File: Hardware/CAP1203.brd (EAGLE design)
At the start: 38.1 x 25.4 mm, 41 parts, among them J1 Qwiic Right Angle, J2 Qwiic Right Angle, J3 Cap Touch Breakout Pins, J4 I2C Breakout Pins, U1 Cap Touch Slider, U2 CAP1203

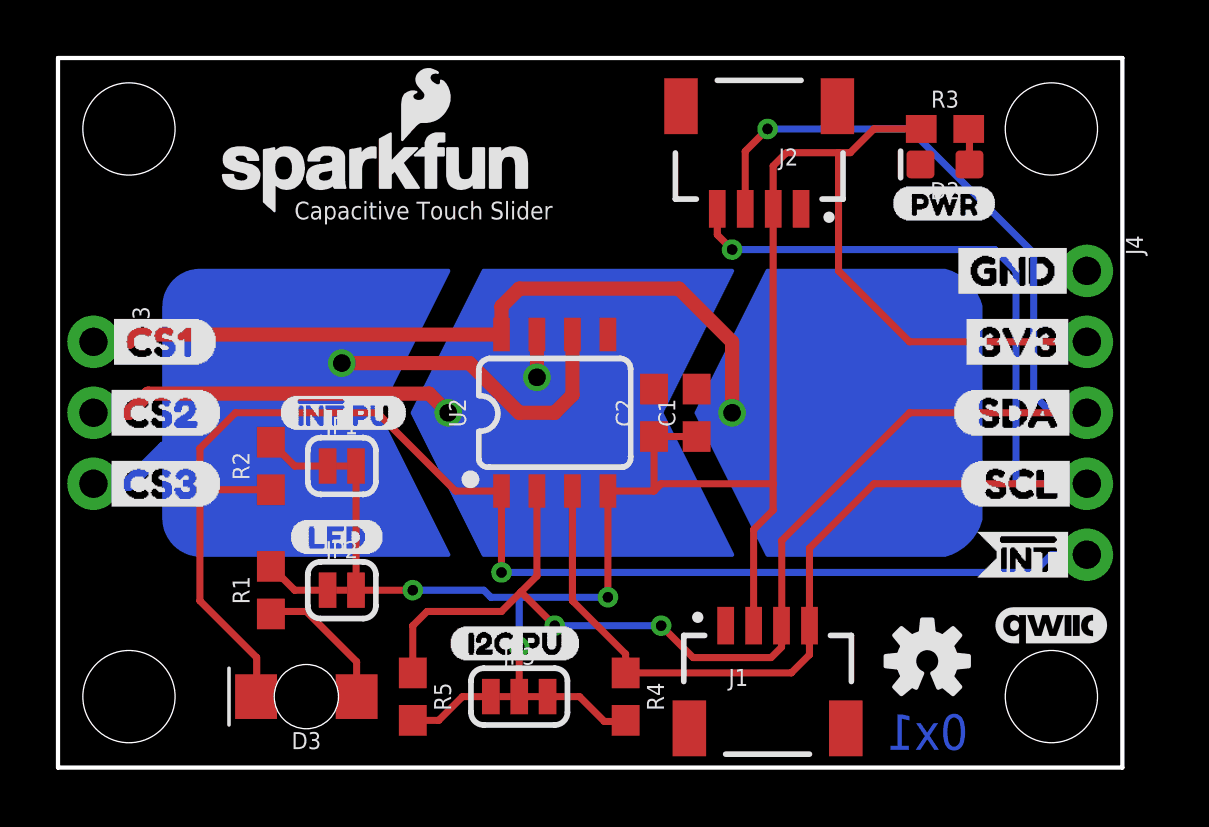
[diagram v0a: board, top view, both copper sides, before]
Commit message: Design review revisions
* Updated brd and sch to match SparkFun design standards
* Updated symbol to depict slider
* Updated silkscreen text
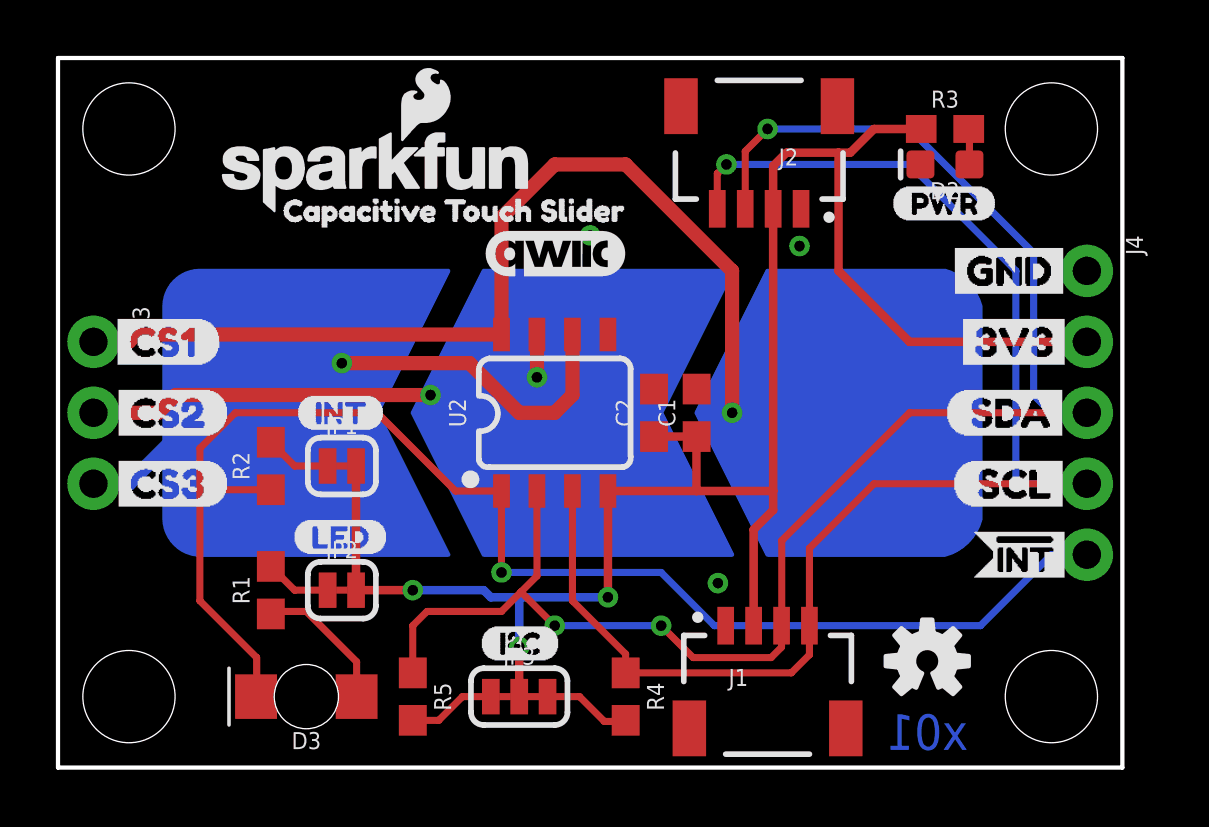
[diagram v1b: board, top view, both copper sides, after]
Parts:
- added U$17: QWIIC_LOGO_5MM, SparkFun-Aesthetics:QWIIC_5MM
- added U$3, U$5: (no value), buzzard_labels_title:CAPACITIVE_TOUCH_SLIDER0
- S1: value Cap Touch Slider -> (none)
- U$13: device buzzard_labels:PWR0 -> Labels:I_SUPER2_C-()-03
- U$14: device buzzard_labels:I2C_PU1 -> buzzard_labels (4):INT0
- U$15: device buzzard_labels (1):#INT#_PU1 -> Labels:PWR-()-03
- U$4: value (none) -> QWIIC_LOGO_5MM; device SparkFun-Aesthetics:QWIIC_4MM -> SparkFun-Aesthetics:QWIIC_5MM
- U$6: device SparkFun-Aesthetics:QWIIC_4MM -> buzzard_labels (5):ACT0
- moved U$6 24.9 mm to (10.7, 4.57), flipped to the bottom
- moved U$15 23.5 mm to (29.8, 20.2)
- moved U$13 21.6 mm to (15.1, 4.45)
- moved U$4 10.2 mm to (25.4, 3.81)
- moved U$14 9.90 mm to (8.51, 12.7)
- moved U$8 0.25 mm to (32.0, 10.2)
- moved U$11 0.25 mm to (1.65, 12.7)
- moved U$12 0.25 mm to (1.65, 10.2)
- moved U$9 0.25 mm to (31.8, 12.7)
- moved U$7 0.13 mm to (32.5, 7.62)
- moved U$10 0.13 mm to (1.65, 15.2)
- moved U$1 0.13 mm to (31.9, 15.2)
- moved U$16 0.13 mm to (8.38, 8.26)
- moved U$2 0.13 mm to (31.6, 17.8)
- renumbered U1 to S1
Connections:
- net INT renamed !INT
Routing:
- net CS1: track 31.4 -> 38.4 mm
- net CS2: track 20.3 -> 24.3 mm
- net !INT: track 48.9 -> 50.5 mm
- net SCL: track 51.2 -> 52.7 mm
- added copper zone on layer 1, net GND
- added copper zone on layer 16, net GND
- removed copper zone on layer 16, net N$7
- removed copper zone on layer 1, net N$8
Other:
- board text added: "x01"
- board text removed: "0x1"
- board text removed: "Capacitive Touch Slider"
